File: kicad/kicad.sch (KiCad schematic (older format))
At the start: 6 parts, among them U1 LT1963

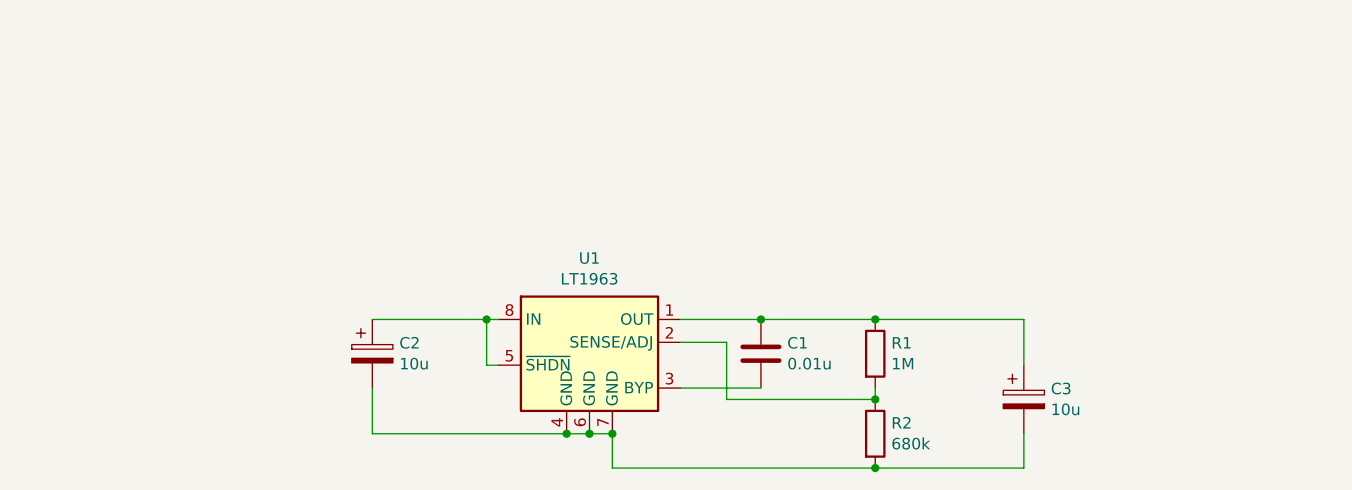
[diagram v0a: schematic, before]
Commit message: Footprints and symbols for charger, updated schematic.
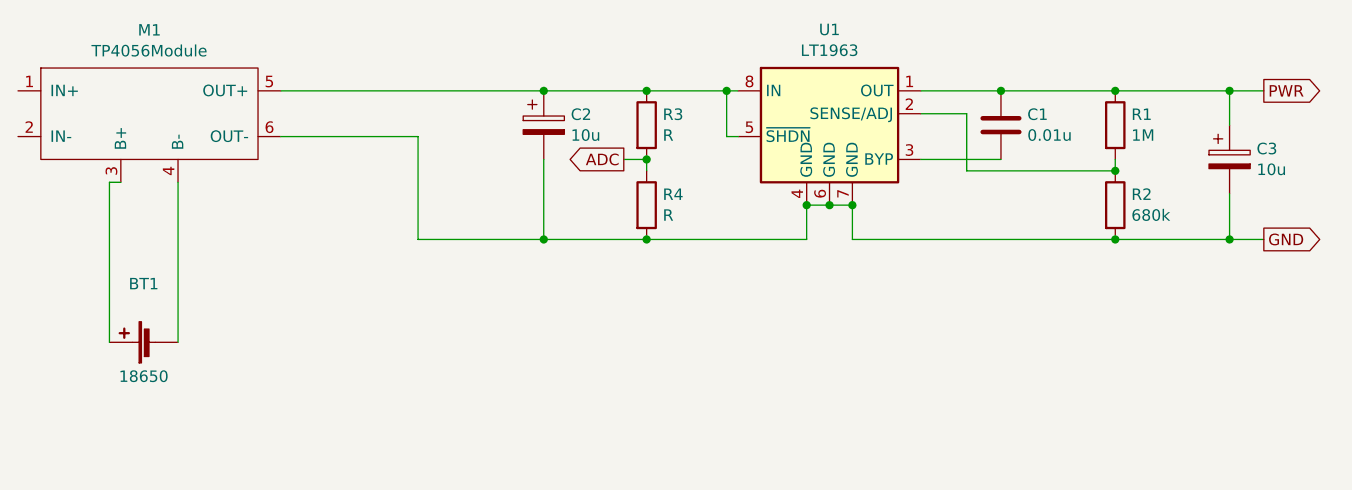
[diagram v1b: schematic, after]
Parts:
- added BT1: 18650, Battery:BatteryHolder_MPD_BH-18650-PC2, symbol Device:Battery_Cell
- added M1: TP4056Module, footprints:TP4056_Module, symbol projectlib:TP4056Module
- added R3, R4: R, Resistor_SMD:R_1206_3216Metric, symbol Device:R
- C1: footprint (none) -> Capacitor_SMD:C_1206_3216Metric_Pad1.42x1.75mm_HandSolder
- C2, C3: footprint (none) -> Capacitor_THT:CP_Radial_D5.0mm_P2.50mm
- R1, R2: footprint (none) -> Resistor_SMD:R_1206_3216Metric
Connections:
- net PWR: now reaches C1.1, C3.1, R1.1, U1.1 (OUT)
- net GND: now reaches C2.2, C3.2, R2.2, U1.4 (GND), U1.6 (GND), U1.7 (GND)
- net GND: now also M1.6 (OUT-), R4.2
- net at C2.1, U1.5 (~SHDN), U1.8 (IN): now also M1.5 (OUT+), R3.1
- new net: BT1.1 (+), M1.3 (B+)
- new net: BT1.2 (-), M1.4 (B-)
- new net ADC: R3.2, R4.1
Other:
- moved on the sheet: C1, C2, C3, R1, R2, U1
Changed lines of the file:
@@
 L lt1763:LT1963 U1
 U 1 1 5D66AE48
-P 3300 2100
-F 0 "U1" H 3300 2567 50  0000 C CNN
-F 1 "LT1963" H 3300 2476 50  0000 C CNN
-F 2 "Package_SO:SO-8_3.9x4.9mm_P1.27mm" H 3300 1350 50  0001 C CNN
-F 3 "https://www.analog.com/media/en/technical-documentation/data-sheets/1763fh.pdf" H 3300 1550 50  0001 C CNN
-	1    3300 2100
+P 4350 1100
+F 0 "U1" H 4350 1567 50  0000 C CNN
+F 1 "LT1963" H 4350 1476 50  0000 C CNN
+F 2 "Package_SO:SO-8_3.9x4.9mm_P1.27mm" H 4350 350 50  0001 C CNN
+F 3 "https://www.analog.com/media/en/technical-documentation/data-sheets/1763fh.pdf" H 4350 550 50  0001 C CNN
+	1    4350 1100
 	1    0    0    -1
 $EndComp
@@
 L Device:C C1
 U 1 1 5D66BDA0
-P 4050 2050
-F 0 "C1" H 4165 2096 50  0000 L CNN
-F 1 "0.01u" H 4165 2005 50  0000 L CNN
-F 2 "" H 4088 1900 50  0001 C CNN
-F 3 "~" H 4050 2050 50  0001 C CNN
-	1    4050 2050
-	1    0    0    -1
-$EndComp
+P 5100 1050
+F 0 "C1" H 5215 1096 50  0000 L CNN
+F 1 "0.01u" H 5215 1005 50  0000 L CNN
+F 2 "Capacitor_SMD:C_1206_3216Metric_Pad1.42x1.75mm_HandSolder" H 5138 900 50  0001 C CNN
+F 3 "~" H 5100 1050 50  0001 C CNN
+	1    5100 1050
+	1    0    0    -1
+$EndComp
+Wire Wire Line
+	4750 900  5100 900
+Wire Wire Line
+	4750 1200 5100 1200
+Wire Wire Line
+	3900 900  3900 1100
+Wire Wire Line
+	3900 1100 3950 1100
+Connection ~ 3900 900
+Wire Wire Line
+	3900 900  3950 900
+Wire Wire Line
+	4250 1400 4350 1400
+Wire Wire Line
+	4350 1400 4450 1400
+Connection ~ 4350 1400
+$Comp
+L Device:R R1
+U 1 1 5D66D87C
+P 5600 1050
+F 0 "R1" H 5670 1096 50  0000 L CNN
+F 1 "1M" H 5670 1005 50  0000 L CNN
+F 2 "Resistor_SMD:R_1206_3216Metric" V 5530 1050 50  0001 C CNN
+F 3 "~" H 5600 1050 50  0001 C CNN
+	1    5600 1050
+	1    0    0    -1
+$EndComp
+$Comp
+L Device:R R2
+U 1 1 5D66DD1B
+P 5600 1400
+F 0 "R2" H 5670 1446 50  0000 L CNN
+F 1 "680k" H 5670 1355 50  0000 L CNN
+F 2 "Resistor_SMD:R_1206_3216Metric" V 5530 1400 50  0001 C CNN
+F 3 "~" H 5600 1400 50  0001 C CNN
+	1    5600 1400
+	1    0    0    -1
+$EndComp
+Wire Wire Line
+	5100 900  5600 900
+Connection ~ 5100 900
+Wire Wire Line
+	4750 1000 4950 1000
+Wire Wire Line
+	4950 1000 4950 1250
+Wire Wire Line
+	4950 1250 5600 1250
+Wire Wire Line
+	5600 1250 5600 1200
+Connection ~ 5600 1250
+Wire Wire Line
+	5600 1550 4450 1550
+Wire Wire Line
+	4450 1550 4450 1400
+Connection ~ 4450 1400
+$Comp
+L Device:CP C3
+U 1 1 5D66F7C0
+P 6100 1200
+F 0 "C3" H 6218 1246 50  0000 L CNN
+F 1 "10u" H 6218 1155 50  0000 L CNN
+F 2 "Capacitor_THT:CP_Radial_D5.0mm_P2.50mm" H 6138 1050 50  0001 C CNN
+F 3 "~" H 6100 1200 50  0001 C CNN
+	1    6100 1200
+	1    0    0    -1
+$EndComp
+Wire Wire Line
+	5600 900  6100 900
+Wire Wire Line
+	6100 900  6100 1050
+Connection ~ 5600 900
+Wire Wire Line
+	5600 1550 6100 1550
+Wire Wire Line
+	6100 1550 6100 1350
+Connection ~ 5600 1550
 $Comp
 L Device:CP C2
 U 1 1 5D66CA68
-P 2350 2050
-F 0 "C2" H 2468 2096 50  0000 L CNN
-F 1 "10u" H 2468 2005 50  0000 L CNN
-F 2 "" H 2388 1900 50  0001 C CNN
-F 3 "~" H 2350 2050 50  0001 C CNN
-	1    2350 2050
-	1    0    0    -1
-$EndComp
-Wire Wire Line
-	3700 1900 4050 1900
-Wire Wire Line
-	3700 2200 4050 2200
-Wire Wire Line
-	2350 1900 2850 1900
-Wire Wire Line
-	2850 1900 2850 2100
-Wire Wire Line
-	2850 2100 2900 2100
-Connection ~ 2850 1900
-Wire Wire Line
-	2850 1900 2900 1900
-Wire Wire Line
-	2350 2200 2350 2400
-Wire Wire Line
-	2350 2400 3200 2400
-Wire Wire Line
-	3200 2400 3300 2400
-Connection ~ 3200 2400
-Wire Wire Line
-	3300 2400 3400 2400
-Connection ~ 3300 2400
-$Comp
-L Device:R R1
-U 1 1 5D66D87C
-P 4550 2050
-F 0 "R1" H 4620 2096 50  0000 L CNN
-F 1 "1M" H 4620 2005 50  0000 L CNN
-F 2 "" V 4480 2050 50  0001 C CNN
-F 3 "~" H 4550 2050 50  0001 C CNN
-	1    4550 2050
-	1    0    0    -1
-$EndComp
-$Comp
-L Device:R R2
-U 1 1 5D66DD1B
-P 4550 2400
-F 0 "R2" H 4620 2446 50  0000 L CNN
-F 1 "680k" H 4620 2355 50  0000 L CNN
-F 2 "" V 4480 2400 50  0001 C CNN
-F 3 "~" H 4550 2400 50  0001 C CNN
-	1    4550 2400
-	1    0    0    -1
-$EndComp
-Wire Wire Line
-	4050 1900 4550 1900
-Connection ~ 4050 1900
-Wire Wire Line
-	3700 2000 3900 2000
-Wire Wire Line
-	3900 2000 3900 2250
-Wire Wire Line
-	3900 2250 4550 2250
-Wire Wire Line
-	4550 2250 4550 2200
-Connection ~ 4550 2250
-Wire Wire Line
-	4550 2550 3400 2550
-Wire Wire Line
-	3400 2550 3400 2400
-Connection ~ 3400 2400
-$Comp
-L Device:CP C3
-U 1 1 5D66F7C0
-P 5200 2250
-F 0 "C3" H 5318 2296 50  0000 L CNN
-F 1 "10u" H 5318 2205 50  0000 L CNN
-F 2 "" H 5238 2100 50  0001 C CNN
-F 3 "~" H 5200 2250 50  0001 C CNN
-	1    5200 2250
-	1    0    0    -1
-$EndComp
-Wire Wire Line
-	4550 1900 5200 1900
-Wire Wire Line
-	5200 1900 5200 2100
-Connection ~ 4550 1900
-Wire Wire Line
-	5200 2400 5200 2550
-Wire Wire Line
-	5200 2550 4550 2550
-Connection ~ 4550 2550
+P 3100 1050
+F 0 "C2" H 3218 1096 50  0000 L CNN
+F 1 "10u" H 3218 1005 50  0000 L CNN
+F 2 "Capacitor_THT:CP_Radial_D5.0mm_P2.50mm" H 3138 900 50  0001 C CNN
+F 3 "~" H 3100 1050 50  0001 C CNN
+	1    3100 1050
+	1    0    0    -1
+$EndComp
+Wire Wire Line
+	3100 900  3550 900
+$Comp
+L Device:R R3
+U 1 1 5D68000D
+P 3550 1050
+F 0 "R3" H 3620 1096 50  0000 L CNN
+F 1 "R" H 3620 1005 50  0000 L CNN
+F 2 "Resistor_SMD:R_1206_3216Metric" V 3480 1050 50  0001 C CNN
+F 3 "~" H 3550 1050 50  0001 C CNN
+	1    3550 1050
+	1    0    0    -1
+$EndComp
+Connection ~ 3550 900
+Wire Wire Line
+	3550 900  3900 900
+$Comp
+L Device:R R4
+U 1 1 5D68063C
+P 3550 1400
+F 0 "R4" H 3620 1446 50  0000 L CNN
+F 1 "R" H 3620 1355 50  0000 L CNN
+F 2 "Resistor_SMD:R_1206_3216Metric" V 3480 1400 50  0001 C CNN
+F 3 "~" H 3550 1400 50  0001 C CNN
+	1    3550 1400
+	1    0    0    -1
+$EndComp
+Wire Wire Line
+	4250 1400 4250 1550
+Wire Wire Line
+	4250 1550 3550 1550
+Connection ~ 4250 1400
+Connection ~ 3550 1550
+Wire Wire Line
+	3100 1200 3100 1550
+Wire Wire Line
+	3550 1200 3550 1250
+Text GLabel 3450 1200 0    50   Output ~ 0
+ADC
+Wire Wire Line
+	3450 1200 3550 1200
+Connection ~ 3550 1200
+$Comp
+L projectlib:TP4056Module M1
+U 1 1 5D68A11D
+P 1350 1000
+F 0 "M1" H 1375 1365 50  0000 C CNN
+F 1 "TP4056Module" H 1375 1274 50  0000 C CNN
+F 2 "footprints:TP4056_Module" H 1350 1000 50  0001 C CNN
+F 3 "" H 1350 1000 50  0001 C CNN
+	1    1350 1000
+	1    0    0    -1
+$EndComp
+Wire Wire Line
+	1950 900  3100 900
+Connection ~ 3100 900
+Wire Wire Line
+	1950 1100 2550 1100
+Wire Wire Line
+	2550 1100 2550 1550
+Wire Wire Line
+	2550 1550 3100 1550
+Connection ~ 3100 1550
+Wire Wire Line
+	3100 1550 3550 1550
+$Comp
+L Device:Battery_Cell BT1
+U 1 1 5D6973D2
+P 1400 2000
+F 0 "BT1" V 1655 2050 50  0000 C CNN
+F 1 "18650" V 1250 2050 50  0000 C CNN
+F 2 "Battery:BatteryHolder_MPD_BH-18650-PC2" V 1400 2060 50  0001 C CNN
+F 3 "~" V 1400 2060 50  0001 C CNN
+	1    1400 2000
+	0    -1   -1   0
+$EndComp
+Wire Wire Line
+	1200 2000 1200 1300
+Wire Wire Line
+	1200 1300 1250 1300
+Wire Wire Line
+	1500 1300 1500 2000
+Text GLabel 6250 900  2    50   Output ~ 0
+PWR
+Text GLabel 6250 1550 2    50   Output ~ 0
+GND
+Wire Wire Line
+	6250 1550 6100 1550
+Connection ~ 6100 1550
+Wire Wire Line
+	6250 900  6100 900
+Connection ~ 6100 900
 $EndSCHEMATC

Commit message: WIP
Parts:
- added C4: 0.01u, Capacitor_SMD:C_1206_3216Metric, symbol Device:C
- added C5: 470u, Capacitor_THT:CP_Radial_D5.0mm_P2.50mm, symbol Device:CP
- added J1: Prog Pads, Connector_PinHeader_2.54mm:PinHeader_1x05_P2.54mm_Vertical, symbol Connector_Generic:Conn_01x05
- added J2: SLP, Connector_PinHeader_2.54mm:PinHeader_1x02_P2.54mm_Vertical, symbol Connector_Generic:Conn_02x01
- added J3: SHT21, Connector_PinSocket_2.54mm:PinSocket_1x04_P2.54mm_Vertical, symbol Connector_Generic:Conn_01x04
- added J4: BH1750, Connector_PinSocket_2.54mm:PinSocket_1x05_P2.54mm_Vertical, symbol Connector_Generic:Conn_01x05
- added R10, R9: 470, Resistor_SMD:R_1206_3216Metric, symbol Device:R
- added R5, R6, R7, R8: 10k, Resistor_SMD:R_1206_3216Metric, symbol Device:R
- added SW1: RST, Button_Switch_SMD:SW_Push_SPST_NO_Alps_SKRK, symbol Switch:SW_Push
- added SW2: PRG, Button_Switch_SMD:SW_Push_SPST_NO_Alps_SKRK, symbol Switch:SW_Push
- added U2: ESP-12F, RF_Module:ESP-12E, symbol RF_Module:ESP-12F
- R3: value R -> 1M
- R4: value R -> 220k
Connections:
- net ADC: now also U2.2 (ADC)
- net GND: now also C4.2, C5.2, J1.5 (Pin_5), J2.1 (Pin_1), J3.2 (Pin_2), J4.2 (Pin_2), R10.2, R8.2, R9.2, U2.15 (GND), U2.4 (GPIO16)
- net PWR: now also C4.1, C5.1, J3.1 (Pin_1), J4.1 (Pin_1), R5.1, R6.1, R7.1, U2.8 (VCC)
- new net: R8.1, U2.16 (GPIO15)
- new net: R5.2, U2.3 (EN)
- new net: R10.1, SW1.2
- new net: R9.1, SW2.2
- new net DTR: J1.4 (Pin_4), R7.2, SW2.1, U2.18 (GPIO0)
- new net RST: J1.1 (Pin_1), J2.2 (Pin_2), R6.2, SW1.1, U2.1 (~RST)
- new net RXD: J1.3 (Pin_3), U2.21 (GPIO3/RXD)
- new net SCL: J3.3 (Pin_3), J4.3 (Pin_3), U2.20 (GPIO5)
- new net SDA: J3.4 (Pin_4), J4.4 (Pin_4), U2.19 (GPIO4)
- new net TXD: J1.2 (Pin_2), U2.22 (GPIO1/TXD)
- no-connect marks 0 -> 13
